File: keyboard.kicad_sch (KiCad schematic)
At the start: 33 parts, among them IC2 Intel 80C51, IC3 74LS145, IC4 74LS145, IC7 74LS366, IC9 74LS241

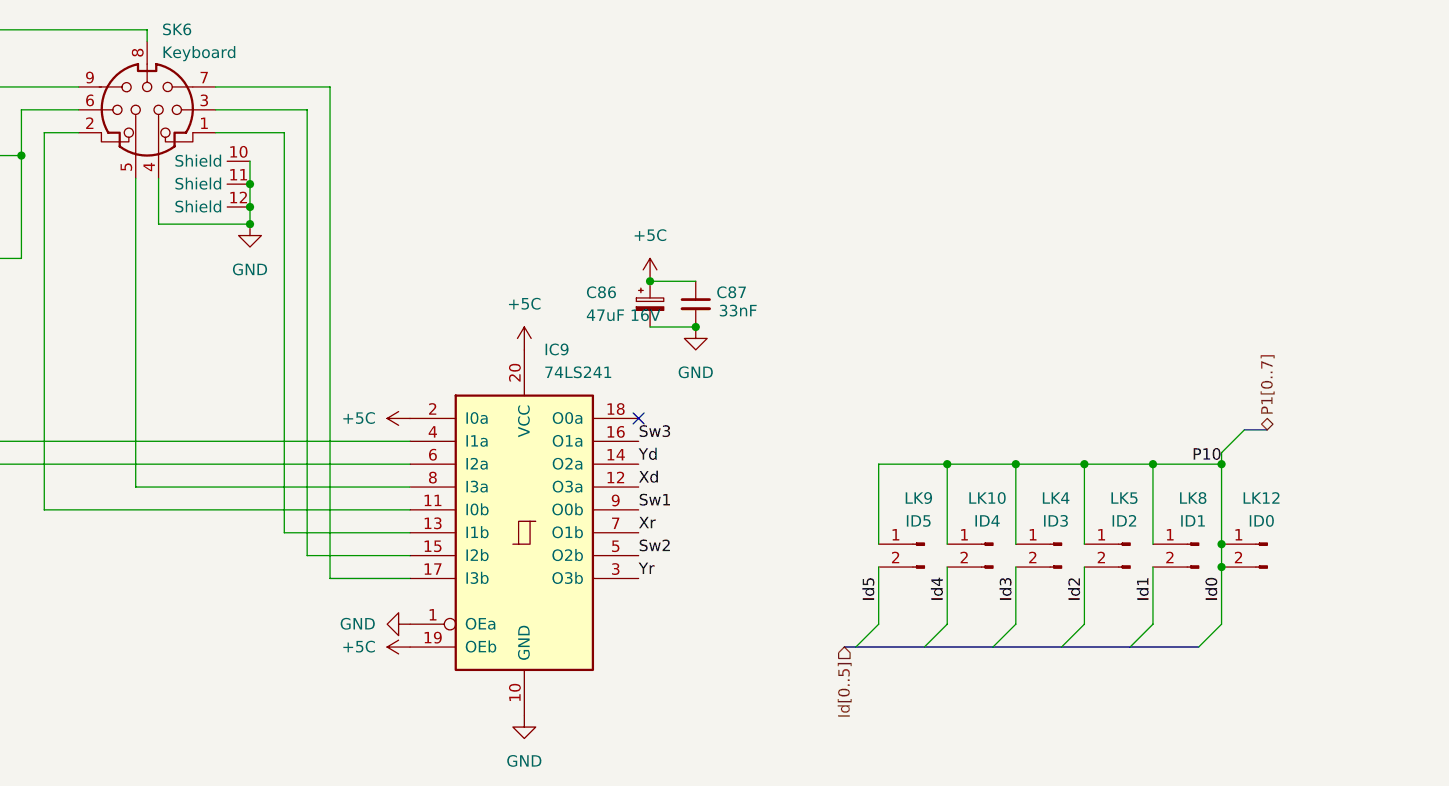
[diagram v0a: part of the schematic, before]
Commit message: turn LK12 into net tie, fix remaining DRC faults
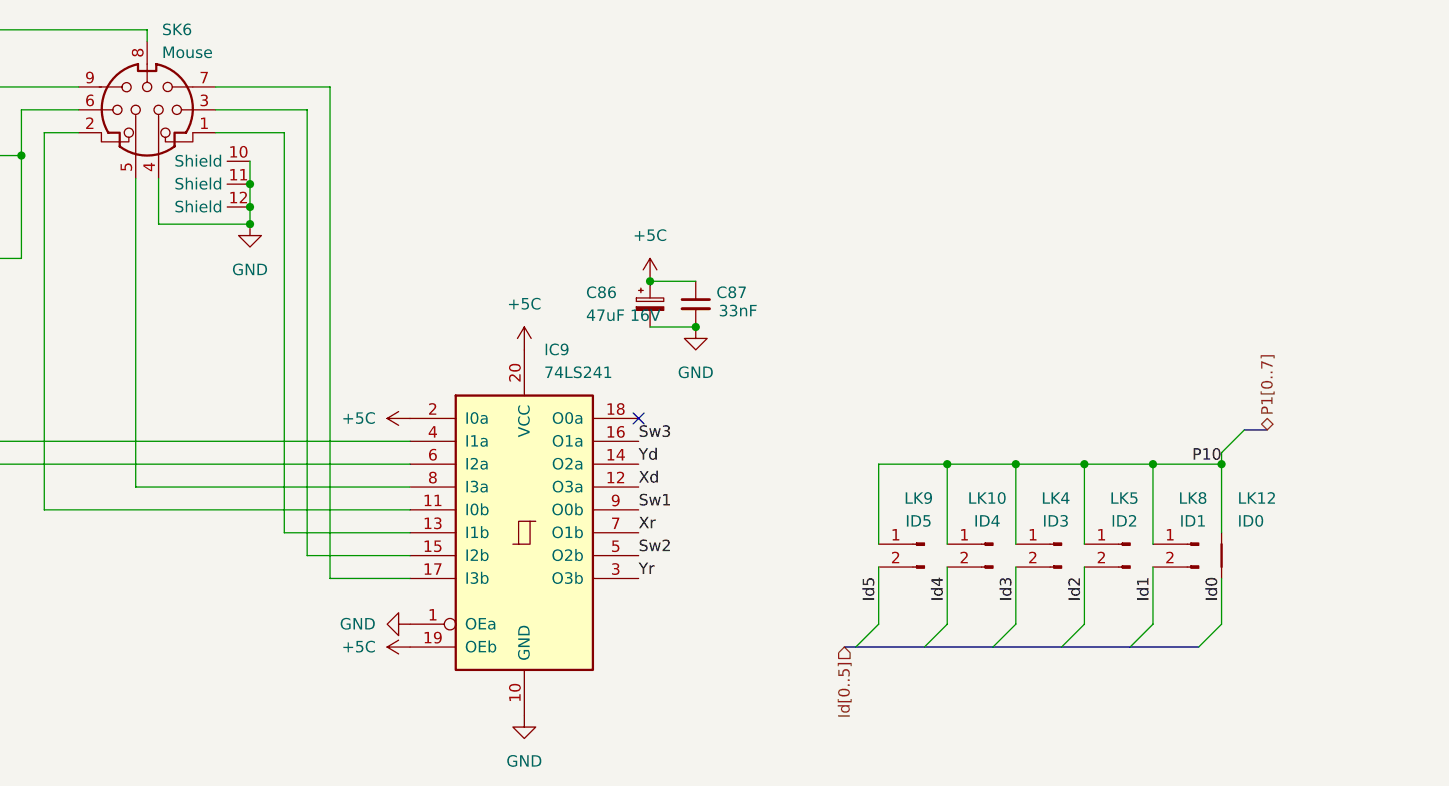
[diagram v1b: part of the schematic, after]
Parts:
- removed LK12: ID0, Acorn:Link, symbol Connector:Conn_01x02_Pin
- added LK12: ID0, Acorn:Link_Connected, symbol Device:NetTie_2
- SK6: value Keyboard -> Mouse
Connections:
- net Id0: now also LK12.2; no longer IC2.2 (P10), LK10.1 (Pin_1), LK4.1 (Pin_1), LK5.1 (Pin_1), LK8.1 (Pin_1), LK9.1 (Pin_1), SK2.19 (Pin_19)
- new net P10: IC2.2 (P10), LK10.1 (Pin_1), LK12.1, LK4.1 (Pin_1), LK5.1 (Pin_1), LK8.1 (Pin_1), LK9.1 (Pin_1), SK2.19 (Pin_19)
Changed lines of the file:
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@@
 	)
 	(junction
-		(at 179.07 104.14)
-		(diameter 0)
-		(color 0 0 0 0)
-	)
-	(junction
 		(at 71.12 66.04)
 		(diameter 0)
@@
 	)
 	(junction
-		(at 179.07 101.6)
-		(diameter 0)
-		(color 0 0 0 0)
-	)
-	(junction
 		(at 96.52 177.8)
 		(diameter 0)
@@
 	(wire
 		(pts
-			(xy 179.07 92.71) (xy 179.07 101.6)
-		)
-		(stroke
-			(width 0)
-			(type default)
-		)
-	)
-	(wire
-		(pts
 			(xy 254 151.13) (xy 254 171.45)
 		)
@@
 	(wire
 		(pts
-			(xy 179.07 101.6) (xy 179.07 104.14)
-		)
-		(stroke
-			(width 0)
-			(type default)
-		)
-	)
-	(wire
-		(pts
 			(xy 90.17 182.88) (xy 104.14 182.88)
 		)
@@
 	(wire
 		(pts
-			(xy 179.07 104.14) (xy 179.07 110.49)
+			(xy 179.07 105.41) (xy 179.07 110.49)
 		)
 		(stroke
@@
 	(wire
 		(pts
+			(xy 179.07 92.71) (xy 179.07 100.33)
+		)
+		(stroke
+			(width 0)
+			(type default)
+		)
+	)
+	(wire
+		(pts
 			(xy 100.33 170.18) (xy 104.14 170.18)
 		)
@@
 			)
 		)
-		(property "Value" "Keyboard"
+		(property "Value" "Mouse"
 			(at 61.3411 46.99 0)
 			(effects
@@
 	)
 	(symbol
-		(lib_id "Connector:Conn_01x02_Pin")
-		(at 184.15 101.6 0)
-		(mirror y)
-		(unit 1)
-		(exclude_from_sim no)
-		(in_bom yes)
-		(on_board yes)
-		(dnp no)
-		(property "Reference" "LK12"
-			(at 183.515 96.52 0)
-			(effects
-				(font
-					(size 1.27 1.27)
-				)
-			)
-		)
-		(property "Value" "ID0"
-			(at 183.515 99.06 0)
-			(effects
-				(font
-					(size 1.27 1.27)
-				)
-			)
-		)
-		(property "Footprint" "Acorn:Link"
-			(at 184.15 101.6 0)
-			(effects
-				(font
-					(size 1.27 1.27)
-				)
-				(hide yes)
-			)
-		)
-		(property "Datasheet" "~"
-			(at 184.15 101.6 0)
-			(effects
-				(font
-					(size 1.27 1.27)
-				)
-				(hide yes)
-			)
-		)
-		(property "Description" "Generic connector, single row, 01x02, script generated"
-			(at 184.15 101.6 0)
-			(effects
-				(font
-					(size 1.27 1.27)
-				)
-				(hide yes)
-			)
-		)
-		(pin "2"
-		)
-		(pin "1"
-		)
-		(instances
-			(project "Acorn-A3010"
-				(path "/999882f3-94f8-4a89-9093-27a47d0cb289/20613dd3-c886-4190-96bd-e62e2e571bea"
-					(reference "LK12")
-					(unit 1)
-				)
-			)
-		)
-	)
-	(symbol
 		(lib_id "74xx:74LS145")
 		(at 179.07 194.31 0)
@@
 					(unit 1)
 				)
+			)
+		)
+	)
+	(symbol
+		(lib_id "Device:NetTie_2")
+		(at 179.07 102.87 90)
+		(mirror x)
+		(unit 1)
+		(exclude_from_sim no)
+		(in_bom no)
+		(on_board yes)
+		(dnp no)
+		(property "Reference" "LK12"
+			(at 180.848 96.52 90)
+			(effects
+				(font
+					(size 1.27 1.27)
+				)
+				(justify right)
+			)
+		)
+		(property "Value" "ID0"
+			(at 180.848 99.06 90)
+			(effects
+				(font
+					(size 1.27 1.27)
+				)
+				(justify right)
+			)
+		)
+		(property "Footprint" "Acorn:Link_Connected"
+			(at 179.07 102.87 0)
+			(effects
+				(font
+					(size 1.27 1.27)
+				)
+				(hide yes)
+			)
+		)
+		(property "Datasheet" "~"
+			(at 179.07 102.87 0)
+			(effects
+				(font
+					(size 1.27 1.27)
+				)
+				(hide yes)
+			)
+		)
+		(property "Description" "Net tie, 2 pins"
+			(at 179.07 102.87 0)
+			(effects
+				(font
+					(size 1.27 1.27)
+				)
+				(hide yes)
+			)
+		)
+		(pin "1"
+		)
+		(pin "2"
+		)
+		(instances
+			(project "Acorn-A3010"
+				(path "/999882f3-94f8-4a89-9093-27a47d0cb289/20613dd3-c886-4190-96bd-e62e2e571bea"
+					(reference "LK12")
+					(unit 1)
+				)

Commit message: use handsolder footprints for fuses
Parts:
- FS5: footprint Fuse:Fuse_2512_6332Metric -> Fuse:Fuse_2512_6332Metric_Pad1.52x3.35mm_HandSolder
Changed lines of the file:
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@@
 			)
 		)
-		(property "Footprint" "Fuse:Fuse_2512_6332Metric"
+		(property "Footprint" "Fuse:Fuse_2512_6332Metric_Pad1.52x3.35mm_HandSolder"
 			(at 39.37 68.58 0)
 			(effects

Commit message: V0.3 fabrication
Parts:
- added LK1: DEL, Acorn:Link, symbol Connector:Conn_01x02_Pin
- added SW3: DEL, Button_Switch_SMD:SW_SPST_TS-1088-xR020, symbol Switch:SW_Push
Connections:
- net P04: now also LK1.2 (Pin_2), SW3.1
- net Y8: now also LK1.1 (Pin_1), SW3.2
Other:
- note added: "Keyboard Ribbon Connectors"
- moved on the sheet: LK7, SK2, SK3

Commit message: adjust audio jack footprint
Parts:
- SW3: DigiKey (none) -> SKRKAEE020; LCSC (none) -> C720477
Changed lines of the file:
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@@
+			)
+		)
+		(property "LCSC" "C720477"
+			(at 337.82 113.03 0)
+			(effects
+				(font
+					(size 1.27 1.27)
+				)
+				(hide yes)
+			)
+		)
+		(property "DigiKey" "SKRKAEE020"
+			(at 337.82 113.03 0)
+			(effects
+				(font
+					(size 1.27 1.27)
+				)
+				(hide yes)
 			)
 		)
